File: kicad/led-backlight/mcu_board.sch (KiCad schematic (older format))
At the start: 10 parts, among them J1 Conn_01x03, Q1 BSS138, U1 AMS1117-3.3, U2 SeeeduinoXIAO

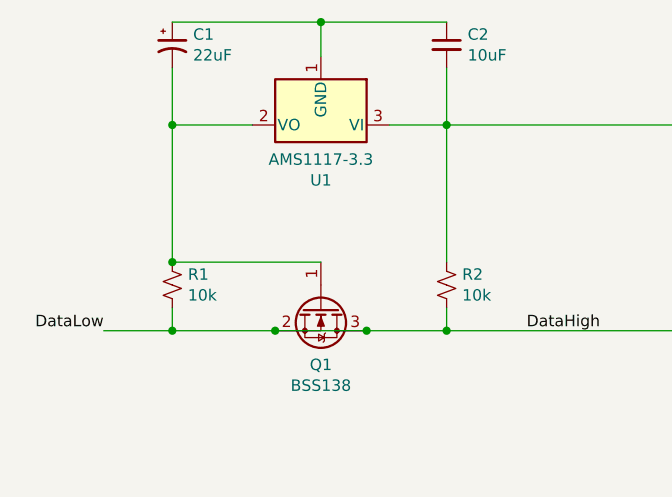
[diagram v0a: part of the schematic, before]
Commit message: add board stackup
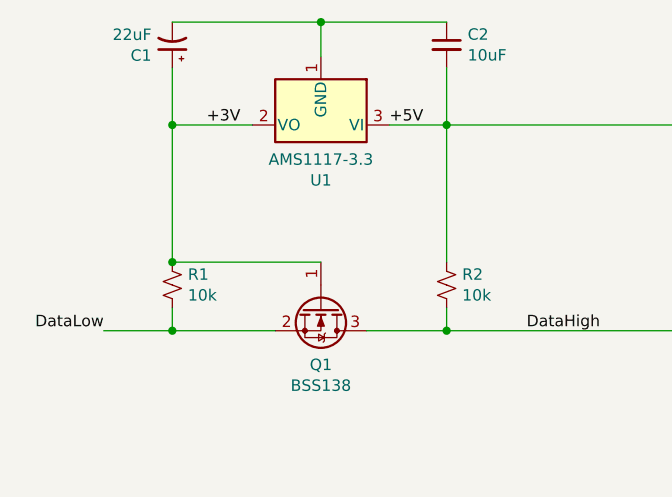
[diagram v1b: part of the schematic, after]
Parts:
- U2: footprint (none) -> Seeeduino XIAO KICAD:Seeeduino XIAO-MOUDLE14P-2.54-21X17.8MM
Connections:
- net +5V: now also C2.2, R2.1, U1.3 (VI), U2.14 (5V)
- net DataHigh: no longer Q1.2 (S), R1.2, U2.11 (PA6_A10_D10_MOSI)
- net at C2.1, U1.1 (GND): now also C1.2; no longer C1.1
- net +3V: now reaches Q1.1 (G), R1.1, U1.2 (VO)
- net +3V: now also C1.1; no longer C1.2
- new net DataLow: Q1.2 (S), R1.2, U2.11 (PA6_A10_D10_MOSI)
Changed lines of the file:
@@
 F 4 "C8020" H 3050 1900 50  0001 C CNN "LCSC Part"
 	1    3050 1900
-	1    0    0    -1
+	-1   0    0    1
 $EndComp
 $Comp
@@
 F 0 "U2" H 5875 3861 50  0000 C CNN
 F 1 "SeeeduinoXIAO" H 5875 3770 50  0000 C CNN
-F 2 "" H 5550 5000 50  0001 C CNN
+F 2 "Seeeduino XIAO KICAD:Seeeduino XIAO-MOUDLE14P-2.54-21X17.8MM" H 5550 5000 50  0001 C CNN
 F 3 "" H 5550 5000 50  0001 C CNN
 F 4 "0" H 5900 4800 50  0001 C CNN "JLCPCB BOM"
@@
 Wire Wire Line
 	3050 3150 3500 3150
-Connection ~ 3500 3150
-Wire Wire Line
-	3500 3150 3900 3150
-Connection ~ 3900 3150
 Wire Wire Line
 	3900 3150 4250 3150
@@
 Wire Wire Line
 	6700 4500 6850 4500
+Text Label 4000 2250 0    50   ~ 0
++5V
+Text Label 3200 2250 0    50   ~ 0
++3V
 $EndSCHEMATC

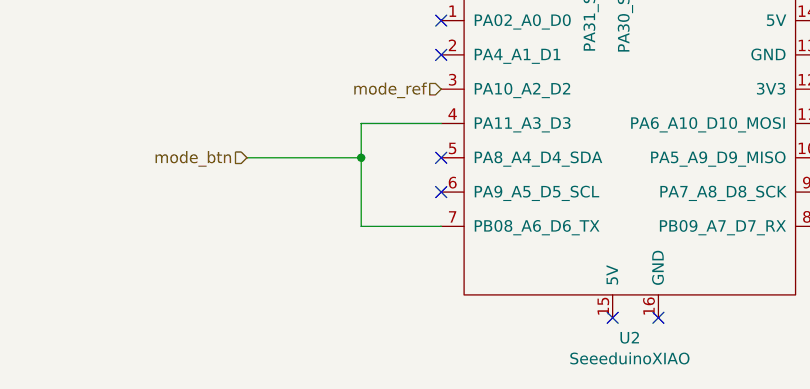
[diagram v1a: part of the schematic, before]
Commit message: add pulldown resistor to eic pin
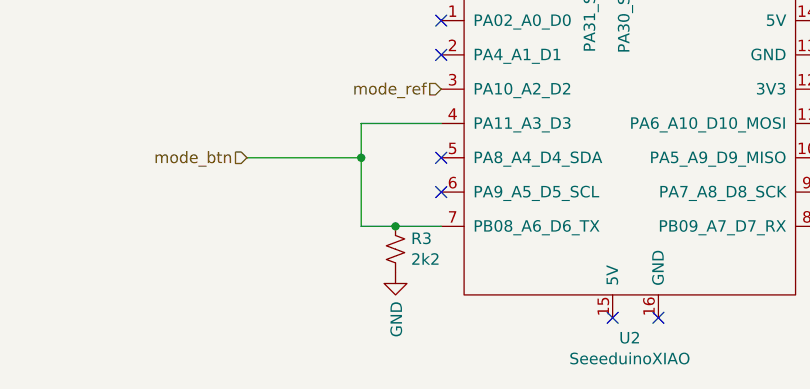
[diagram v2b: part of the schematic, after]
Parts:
- added R3: 2k2, Resistor_SMD:R_0805_2012Metric, symbol Device:R_Small_US
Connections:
- net GND: now also R3.2
- net mode_btn: now also R3.1
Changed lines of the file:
@@
 	4700 4950 4700 5250
 Wire Wire Line
-	4700 5250 5050 5250
+	4700 5250 4850 5250
 Wire Wire Line
 	5050 4800 4700 4800
@@
 Text Label 3200 2250 0    50   ~ 0
 +3V
+$Comp
+L Device:R_Small_US R3
+U 1 1 60F32880
+P 4850 5350
+F 0 "R3" H 4918 5396 50  0000 L CNN
+F 1 "2k2" H 4918 5305 50  0000 L CNN
+F 2 "Resistor_SMD:R_0805_2012Metric" H 4850 5350 50  0001 C CNN
+F 3 "~" H 4850 5350 50  0001 C CNN
+	1    4850 5350
+	1    0    0    -1
+$EndComp
+Connection ~ 4850 5250
+Wire Wire Line
+	4850 5250 5050 5250
+$Comp
+L power:GND #PWR09
+U 1 1 60F32FE4
+P 4850 5450
+F 0 "#PWR09" H 4850 5200 50  0001 C CNN
+F 1 "GND" V 4855 5322 50  0000 R CNN
+F 2 "" H 4850 5450 50  0001 C CNN
+F 3 "" H 4850 5450 50  0001 C CNN
+	1    4850 5450
+	1    0    0    -1
+$EndComp
 $EndSCHEMATC

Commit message: idk can't remember
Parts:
- J1: footprint Connector_JST:JST_XH_S3B-XH-A_1x03_P2.50mm_Horizontal -> initeq:jst_xh_conn_1x03_horizontal
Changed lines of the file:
@@
 F 0 "J1" V 5372 3680 50  0000 L CNN
 F 1 "Conn_01x03" V 5463 3680 50  0000 L CNN
-F 2 "Connector_JST:JST_XH_S3B-XH-A_1x03_P2.50mm_Horizontal" H 5500 3500 50  0001 C CNN
+F 2 "initeq:jst_xh_conn_1x03_horizontal" H 5500 3500 50  0001 C CNN
 F 3 "~" H 5500 3500 50  0001 C CNN
 F 4 "0" H 5500 3500 50  0001 C CNN "JLCPCB BOM"
